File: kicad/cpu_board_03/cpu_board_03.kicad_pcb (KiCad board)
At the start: 4 copper layers, 119.4 x 91.4 mm, 53 parts, among them J1 DIN41612_02x32_AC, J10 PLD_aux, J11 Conn_01x09, J6 Conn_01x02_Socket, J7 Jmp_Irq, J8 Jmp_NMI, J9 Ram1 Enable, SW1 SW_Reset, SW2 SW_PWR, U1 W65C02SxP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

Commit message: routing cpu 3 board
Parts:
- removed J7: Jmp_Irq, Connector_PinHeader_2.54mm:PinHeader_1x02_P2.54mm_Vertical
- removed J8: Jmp_NMI, Connector_PinHeader_2.54mm:PinHeader_1x02_P2.54mm_Vertical
- added C1: 47uF, Capacitor_THT:CP_Radial_D4.0mm_P2.00mm, F.Cu at (122.4, 89.9)
- added R3: 10K, Resistor_SMD:R_0805_2012Metric_Pad1.20x1.40mm_HandSolder, F.Cu at (52.3, 86.4)
- added R5: 10K, Resistor_SMD:R_0805_2012Metric_Pad1.20x1.40mm_HandSolder, F.Cu at (52.3, 88.4)
- C3: footprint Package_SO:SO-20_12.8x7.5mm_P1.27mm -> Capacitor_SMD:C_0805_2012Metric_Pad1.18x1.45mm_HandSolder
- moved SW1 200.6 mm to (26.2, 26.2)
- moved R1 186.5 mm to (33.5, 34.5), turned to -90 degrees
- moved C14 95.8 mm to (87.4, 82.8), turned to -90 degrees
- moved C8 82.0 mm to (71.6, 82.8), turned to -90 degrees
- moved R4 81.0 mm to (41.6, 85.9)
- moved C12 76.0 mm to (129.0, 20.9), turned to -90 degrees
- moved C10 60.4 mm to (-2.56, 74.2)
- moved C3 59.5 mm to (67.1, 79.8), turned to -90 degrees
- moved C7 49.7 mm to (4.06, 84.3)
- moved C11 38.1 mm to (33.9, 90.9)
- moved C4 27.6 mm to (90.9, 17.8), turned to 180 degrees
- moved C6 22.7 mm to (49.3, 17.8), turned to 180 degrees
- moved C5 17.2 mm to (62.5, 17.8), turned to 180 degrees
- moved U9 10.2 mm to (40.6, 63.5)
- moved U10 1.91 mm to (79.4, 86.0)
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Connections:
- J1 pad a10: /AB7 -> VCC
- J1 pad a11: /AB6 -> /AB14
- J1 pad a12: /AB5 -> /AB12
- J1 pad a13: /AB4 -> /AB10
- J1 pad a14: /AB3 -> /AB8
- J1 pad a15: /AB2 -> /AB6
- J1 pad a16: /AB1 -> /AB4
- J1 pad a17: /AB0 -> /AB2
- J1 pad a18: VCC -> /AB0
- J1 pad a2: /AB15 -> /DB6
- J1 pad a21: /~{SYS_CLK} -> unconnected-(J1-Pin_a21-Pada21)
- J1 pad a22: /SYS_CLK -> unconnected-(J1-Pin_a22-Pada22)
- J1 pad a23: /~{IO_SEL} -> /~{IOEN_06}
- J1 pad a24: /~{IOEN_07} -> /~{IOEN_04}
- J1 pad a25: /~{IOEN_06} -> /~{IOEN_02_UART}
- J1 pad a26: /~{IOEN_05} -> /~{IOEN_00_GPIO0}
- J1 pad a27: /~{IOEN_04} -> VCC
- J1 pad a28: /~{IOEN_03} -> unconnected-(J1-Pin_a28-Pada28)
- J1 pad a29: /~{IOEN_02} -> unconnected-(J1-Pin_a29-Pada29)
- J1 pad a3: /AB14 -> /DB4
- J1 pad a30: /~{IOEN_01} -> /~{NMI}
- J1 pad a31: /~{IOEN_00_GPIO0} -> /~{IRQ}
- J1 pad a4: /AB13 -> /DB2
- J1 pad a5: /AB12 -> /DB0
- J1 pad a6: /AB11 -> VCC
- J1 pad a7: /AB10 -> /SYS_CLK
- J1 pad a8: /AB9 -> /~{IO_SEL}
- J1 pad a9: /AB8 -> unconnected-(J1-Pin_a9-Pada9)
- J1 pad c10: unconnected-(J1-Pin_c10-Padc10) -> GND
- J1 pad c11: unconnected-(J1-Pin_c11-Padc11) -> /AB15
- J1 pad c12: unconnected-(J1-Pin_c12-Padc12) -> /AB13
- J1 pad c13: unconnected-(J1-Pin_c13-Padc13) -> /AB11
- J1 pad c14: unconnected-(J1-Pin_c14-Padc14) -> /AB9
- J1 pad c15: unconnected-(J1-Pin_c15-Padc15) -> /AB7
- J1 pad c16: unconnected-(J1-Pin_c16-Padc16) -> /AB5
- J1 pad c17: unconnected-(J1-Pin_c17-Padc17) -> /AB3
- J1 pad c18: GND -> /AB1
- J1 pad c23: unconnected-(J1-Pin_c23-Padc23) -> /~{IOEN_07}
- J1 pad c24: unconnected-(J1-Pin_c24-Padc24) -> /~{IOEN_05}
- J1 pad c25: unconnected-(J1-Pin_c25-Padc25) -> /~{IOEN_03}
- J1 pad c26: unconnected-(J1-Pin_c26-Padc26) -> /~{IOEN_01}
- J1 pad c27: unconnected-(J1-Pin_c27-Padc27) -> GND
- J1 pad c3: /DB6 -> /DB5
- J1 pad c4: /DB5 -> /DB3
- J1 pad c5: /DB4 -> /DB1
- J1 pad c6: /DB3 -> GND
- J1 pad c7: /DB2 -> /~{SYS_CLK}
- J1 pad c8: /DB1 -> /PLD_O7
- J1 pad c9: /DB0 -> /PLD_O0
- U9 pad 7: /CLOCK -> /SYS_CLK
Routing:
- net VCC: track 0.00 -> 268.1 mm
- net /~{IO_SEL}: track 0.00 -> 112.5 mm, vias 0 -> 4
- net /SYS_CLK: track 0.00 -> 100.8 mm, vias 0 -> 4
- net /PLD_O0: track 0.00 -> 77.3 mm
- net /PLD_O7: track 0.00 -> 58.0 mm
- net Net-(U9-~{PB_RST}): track 0.00 -> 52.1 mm
- net /~{SYS_CLK}: track 0.00 -> 51.4 mm
- net /~{RES}: track 0.00 -> 42.3 mm
- net /~{NMI}: track 0.00 -> 34.2 mm
- net /RES: track 0.00 -> 32.7 mm
- net /~{IRQ}: track 0.00 -> 31.8 mm
- net /A6: track 6.13 -> 37.6 mm
- net /A5: track 5.61 -> 35.8 mm
- net /A4: track 5.08 -> 34.3 mm
- net /~{IOEN_00_GPIO0}: track 0.00 -> 22.1 mm
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
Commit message: cleanup and routing
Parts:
- moved C10 64.8 mm to (62.0, 79.8)
- moved U2 8.19 mm to (50.8, 20.3)
- moved C6 8.14 mm to (57.4, 17.3)
- moved U7 7.69 mm to (63.5, 20.3)
- moved C5 7.64 mm to (70.1, 17.3)
- moved U6 4.51 mm to (114.6, 66.2)
- moved U8 4.51 mm to (114.6, 82.4)
- moved H1 4.02 mm to (30.5, 20.3)
- moved H2 1.80 mm to (137.2, 20.3)
- moved C1 1.61 mm to (124.0, 90.4)
- moved SW2 1.61 mm to (226.2, 85.6)
- moved C12 1.61 mm to (130.6, 21.4)
- moved C9 1.61 mm to (221.8, 56.5)
- moved R1 1.61 mm to (35.1, 35.1)
- moved RN1 1.61 mm to (155.8, 47.3)
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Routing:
- net /A12: track 0.00 -> 117.2 mm, vias 0 -> 1
- net /A7: track 6.53 -> 119.9 mm, vias 0 -> 2
- net /A14: track 0.00 -> 102.7 mm, vias 0 -> 2
- net /A13: track 0.00 -> 96.2 mm, vias 0 -> 1
- net /A8: track 6.86 -> 100.5 mm
- net /A11: track 6.55 -> 100.1 mm, vias 0 -> 2
- net /A9: track 6.34 -> 97.3 mm
- net /A10: track 6.02 -> 94.9 mm, vias 0 -> 1
- net /R/~{W}: track 0.00 -> 80.6 mm, vias 0 -> 1
- net /PLD_O0: track 77.3 -> 0.00 mm
- net /A6: track 37.6 -> 114.3 mm, vias 0 -> 2
- net /A5: track 35.8 -> 109.4 mm
- net /A2: track 7.27 -> 76.5 mm
- net /A3: track 6.75 -> 74.8 mm
- net /A4: track 34.3 -> 101.9 mm, vias 0 -> 2
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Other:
- board size 119.4 x 91.4 mm -> 116.8 x 94 mm

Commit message: more routing on cpu board v3
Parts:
- added C13: 100nF, Capacitor_SMD:C_0805_2012Metric_Pad1.18x1.45mm_HandSolder, F.Cu at (118.4, 57.4)
- added C2: 100nF, Capacitor_SMD:C_0805_2012Metric_Pad1.18x1.45mm_HandSolder, F.Cu at (108.2, 17.3)
- moved SW2 187.1 mm to (39.1, 87.9)
- moved D13 176.9 mm to (41.1, 43.2)
- moved R2 176.9 mm to (43.7, 43.2)
- moved C7 116.5 mm to (121.9, 77.7)
- moved C9 101.2 mm to (126.0, 23.9), turned to 0 degrees
- moved J10 98.2 mm to (115.8, 21.8), turned to 90 degrees
- moved J9 92.1 mm to (121.9, 47.2), turned to -90 degrees
- moved D12 41.6 mm to (115.3, 42.2)
- moved RN1 39.4 mm to (129.3, 76.4)
- moved D10 39.2 mm to (117.9, 42.2)
- moved D11 39.2 mm to (120.4, 42.2)
- moved D9 38.3 mm to (122.9, 42.2)
- moved RN3 38.2 mm to (127.0, 41.7), turned to 0 degrees
- moved D1 34.1 mm to (129.0, 73.2), turned to 0 degrees
- moved C12 33.8 mm to (97.0, 16.8)
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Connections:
- RN1 pad 1: Net-(D1-K) -> Net-(D3-K)
- RN1 pad 3: Net-(D3-K) -> Net-(D1-K)
- RN2 pad 2: Net-(D6-K) -> Net-(D8-K)
- RN2 pad 4: Net-(D8-K) -> Net-(D6-K)
- RN3 pad 2: Net-(D11-A) -> Net-(D9-A)
- RN3 pad 3: Net-(D10-A) -> Net-(D11-A)
- RN3 pad 4: Net-(D9-A) -> Net-(D10-A)
- U4 pad 19: /~{CS_RAM0} -> /~{CS_RAM1}
- U4 pad 20: /~{CS_RAM1} -> /~{CS_RAM0}
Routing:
- net GND: track 70.1 -> 685.5 mm, vias 6 -> 18
- net VCC: track 207.4 -> 338.9 mm
- net /PLD_O0: track 0.00 -> 78.8 mm
- net /~{IOEN_00_GPIO0}: track 22.1 -> 98.4 mm, vias 0 -> 6
- net /~{QWE_RAM}: track 0.00 -> 60.8 mm, vias 0 -> 1
- net /A15: track 33.5 -> 92.2 mm, vias 1 -> 2
- net /D0: track 53.2 -> 98.5 mm, vias 0 -> 1
- net /D1: track 53.3 -> 95.6 mm, vias 1 -> 2
- net /D2: track 53.5 -> 92.9 mm, vias 1 -> 2
- net /A14: track 102.7 -> 141.3 mm, vias 2 -> 3
- net /D3: track 62.5 -> 98.7 mm, vias 1 -> 2
- net /CLOCK: track 0.00 -> 36.1 mm, vias 0 -> 1
- net /D4: track 66.5 -> 100.4 mm, vias 1 -> 2
- net /D5: track 71.6 -> 103.1 mm, vias 1 -> 2
- net /D6: track 76.9 -> 105.9 mm, vias 1 -> 2
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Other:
- board size 116.8 x 94 mm -> 104.6 x 92.5 mm

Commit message: more routing
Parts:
- added C15: 100nF, Capacitor_SMD:C_0805_2012Metric_Pad1.18x1.45mm_HandSolder, F.Cu at (52.8, 79.8)
- added U12: 74LS138, Package_SO:SO-16_3.9x9.9mm_P1.27mm, F.Cu at (51.0, 87.0)
- moved R5 16.0 mm to (46.5, 74.7), turned to 0 degrees
- moved R1 15.9 mm to (41.9, 41.7), turned to 180 degrees
- moved R2 15.0 mm to (39.9, 57.7)
- moved D13 14.5 mm to (42.4, 57.7)
- moved R3 12.0 mm to (46.5, 77.5), turned to 0 degrees
- moved C9 10.2 mm to (115.8, 23.9), turned to 90 degrees
- moved SW1 5.15 mm to (43.4, 46.0), turned to -90 degrees
- moved J9 5.06 mm to (116.8, 47.2), turned to 90 degrees
- moved C11 3.01 mm to (40.6, 75.7), turned to 180 degrees
- moved J10 2.26 mm to (115.8, 19.6)
- moved C10 1.08 mm to (62.7, 80.0)
- moved U5 1.05 mm to (61.2, 87.0)
- moved SW2 1.02 mm to (38.1, 87.9), turned to -90 degrees
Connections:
- J1 pad a19: unconnected-(J1-Pin_a19-Pada19) -> VCC
- J1 pad a21: unconnected-(J1-Pin_a21-Pada21) -> /~{IOEN_06}
- J1 pad a22: unconnected-(J1-Pin_a22-Pada22) -> /~{IOEN_04}
- J1 pad a23: /~{IOEN_06} -> /~{IOEN_02_UART}
- J1 pad a24: /~{IOEN_04} -> /~{IOEN_00_GPIO0}
- J1 pad a25: /~{IOEN_02_UART} -> /~{IOEN_14}
- J1 pad a26: /~{IOEN_00_GPIO0} -> /~{IOEN_12}
- J1 pad a27: VCC -> /~{IOEN_10}
- J1 pad a28: unconnected-(J1-Pin_a28-Pada28) -> /~{IOEN_08}
- J1 pad a29: unconnected-(J1-Pin_a29-Pada29) -> VCC
- J1 pad a30: /~{NMI} -> /~{IRQ}
- J1 pad a31: /~{IRQ} -> /~{RES}
- J1 pad c19: unconnected-(J1-Pin_c19-Padc19) -> GND
- J1 pad c21: unconnected-(J1-Pin_c21-Padc21) -> /~{IOEN_07}
- J1 pad c22: unconnected-(J1-Pin_c22-Padc22) -> /~{IOEN_05}
- J1 pad c23: /~{IOEN_07} -> /~{IOEN_03}
- J1 pad c24: /~{IOEN_05} -> /~{IOEN_01}
- J1 pad c25: /~{IOEN_03} -> /~{IOEN_15}
- J1 pad c26: /~{IOEN_01} -> /~{IOEN_13}
- J1 pad c27: GND -> /~{IOEN_11}
- J1 pad c28: unconnected-(J1-Pin_c28-Padc28) -> /~{IOEN_09}
- J1 pad c29: unconnected-(J1-Pin_c29-Padc29) -> GND
- J1 pad c30: /RES -> /~{NMI}
- J1 pad c31: /~{RES} -> /RES
- J1 pad c8: /PLD_O7 -> /~{IO_RD_DIR}
- J10 pad 1: /PLD_I1 -> GND
- J10 pad 2: /PLD_O0 -> /PLD_I1
- J10 pad 3: /PLD_O7 -> VCC
- J9 pad 1: VCC -> GND
- J9 pad 3: GND -> VCC
- U10 pad 1: GND -> VCC
- U11 pad 1: GND -> VCC
- U4 pad 16: /PLD_O7 -> /~{IO_RD_DIR}
- U8 pad 1: unconnected-(U8-A->B-Pad1) -> /~{IO_RD_DIR}
- U8 pad 19: unconnected-(U8-CE-Pad19) -> GND
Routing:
- net VCC: track 338.9 -> 598.9 mm, vias 0 -> 2
- net /~{IO_RD_DIR}: track 0.00 -> 62.7 mm, vias 0 -> 2
- net /PLD_O7: track 58.0 -> 0.00 mm
- net /~{RES}: track 8.08 -> 53.8 mm
- net /RES: track 0.00 -> 31.4 mm
- net /PLD_I1: track 0.00 -> 26.2 mm
- net Net-(U9-~{PB_RST}): track 0.00 -> 23.9 mm
- net /~{IOEN_08}: track 0.00 -> 21.4 mm
- net /~{IOEN_10}: track 0.00 -> 18.6 mm
- net /~{IOEN_12}: track 0.00 -> 16.7 mm
- net /~{IOEN_15}: track 0.00 -> 15.6 mm, vias 0 -> 2
- net /~{IO_SEL}: track 113.9 -> 129.0 mm, vias 4 -> 5
- net /~{IOEN_09}: track 0.00 -> 14.4 mm
- net /A6: track 114.3 -> 127.9 mm, vias 2 -> 3
- net /~{QWE_RAM}: track 60.8 -> 74.3 mm
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
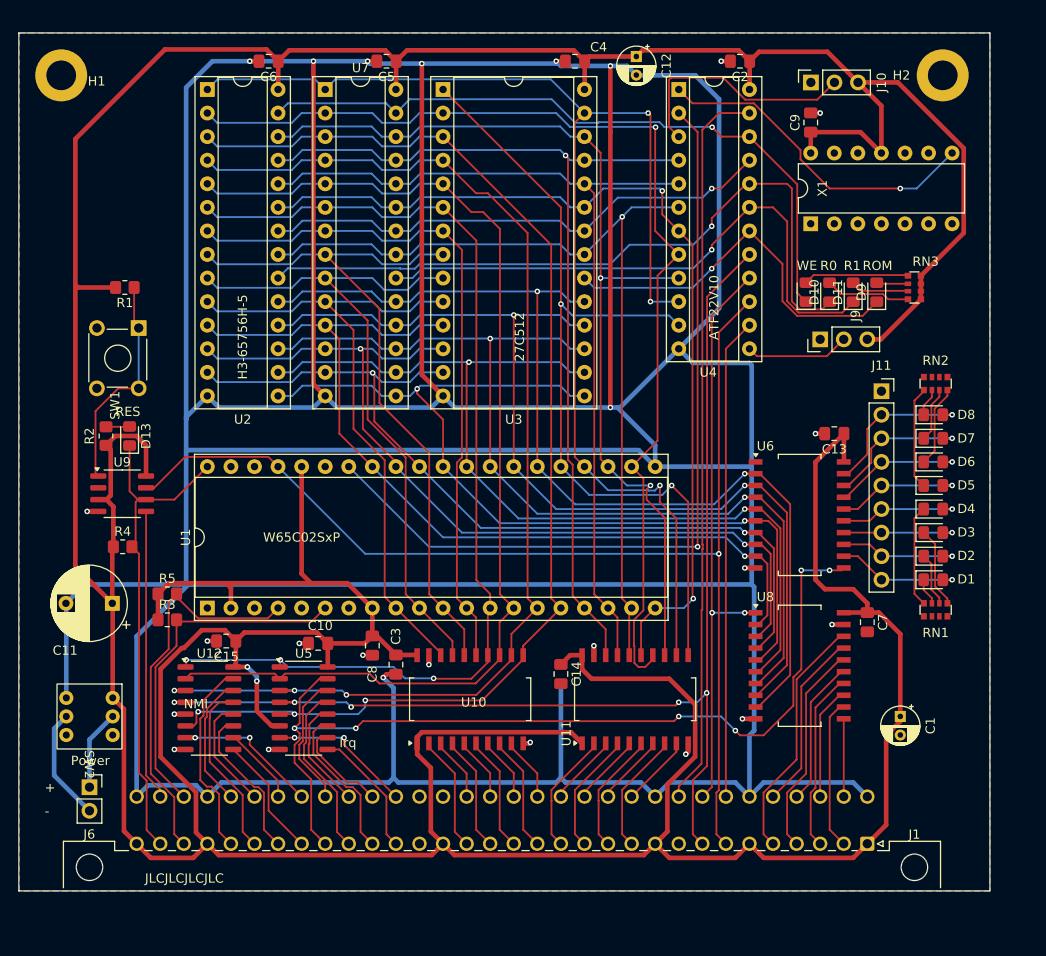
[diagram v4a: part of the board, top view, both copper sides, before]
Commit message: shrink board
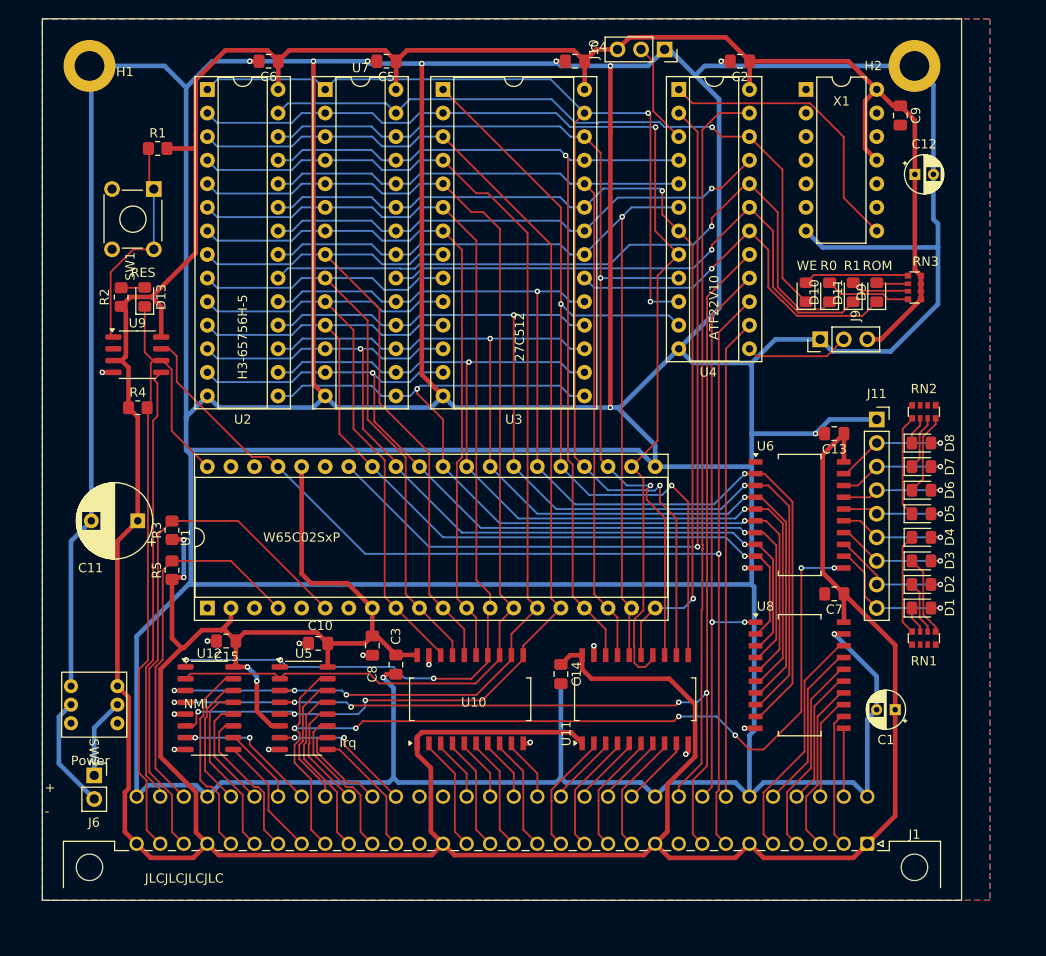
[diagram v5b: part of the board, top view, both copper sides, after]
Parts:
- moved C12 32.6 mm to (127.0, 29.5), turned to 0 degrees
- moved J10 16.2 mm to (100.1, 16.0), turned to -90 degrees
- moved R1 15.4 mm to (45.5, 26.7), turned to 0 degrees
- moved D13 15.1 mm to (44.1, 42.7)
- moved R2 15.1 mm to (41.5, 42.7)
- moved R4 15.1 mm to (43.3, 54.6)
- moved SW1 15.1 mm to (45.0, 31.0)
- moved U9 15.1 mm to (43.3, 48.9)
- moved X1 14.5 mm to (115.3, 20.3), turned to 0 degrees
- moved C9 9.68 mm to (125.5, 23.1), turned to -90 degrees
- moved R3 9.67 mm to (47.0, 67.8), turned to 90 degrees
- moved C11 9.30 mm to (43.3, 66.8)
- moved C7 4.68 mm to (118.4, 74.7), turned to 180 degrees
- moved D5 3.30 mm to (127.8, 66.0)
- moved RN1 3.30 mm to (128.0, 79.4)
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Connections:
- J1 pad a30: /~{IRQ} -> /~{NMI}
- J1 pad c30: /~{NMI} -> /~{IRQ}
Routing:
- net GND: track 676.0 -> 854.2 mm, vias 25 -> 24
- net VCC: track 598.9 -> 548.0 mm, vias 2 -> 4
- net /~{RES}: track 53.8 -> 74.4 mm
- net /~{NMI}: track 37.9 -> 57.7 mm
- net /RES: track 31.4 -> 47.3 mm
- net /PLD_I1: track 26.2 -> 11.1 mm
- net /CLOCK: track 36.1 -> 31.5 mm, vias 1 -> 0
- net /GPIO00_O7: track 16.9 -> 12.8 mm
- net /GPIO00_O6: track 15.7 -> 12.3 mm
- net /SYS_CLK: track 127.8 -> 131.2 mm
- net /GPIO00_O5: track 14.3 -> 11.7 mm
- net /~{CS_RAM0}: track 76.9 -> 74.5 mm
- net /~{IOEN_00_GPIO0}: track 97.6 -> 99.9 mm
- net /GPIO00_O4: track 13.8 -> 11.6 mm
- net /D6: track 105.9 -> 107.9 mm
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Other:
- board size 104.6 x 92.5 mm -> 99.1 x 95 mm

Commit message: DRCs pass...
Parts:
- moved U12 14.5 mm to (65.4, 88.4), turned to 90 degrees
- moved C10 13.9 mm to (49.0, 82.3), turned to 90 degrees
- moved C15 8.52 mm to (61.0, 82.3), turned to 90 degrees
- moved U5 7.83 mm to (53.5, 88.4), turned to 90 degrees
- moved C3 1.61 mm to (67.6, 79.0), turned to 180 degrees
- moved C8 1.44 mm to (70.1, 81.3), turned to 180 degrees
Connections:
- J1 pad a21: /~{IOEN_06} -> /~{IOEN_14}
- J1 pad a22: /~{IOEN_04} -> /~{IOEN_12}
- J1 pad a23: /~{IOEN_02_UART} -> /~{IOEN_10}
- J1 pad a24: /~{IOEN_00_GPIO0} -> /~{IOEN_08}
- J1 pad a25: /~{IOEN_14} -> /~{IOEN_06}
- J1 pad a26: /~{IOEN_12} -> /~{IOEN_04}
- J1 pad a27: /~{IOEN_10} -> /~{IOEN_02_UART}
- J1 pad a28: /~{IOEN_08} -> /~{IOEN_00_GPIO0}
- J1 pad c21: /~{IOEN_07} -> /~{IOEN_15}
- J1 pad c22: /~{IOEN_05} -> /~{IOEN_13}
- J1 pad c23: /~{IOEN_03} -> /~{IOEN_11}
- J1 pad c24: /~{IOEN_01} -> /~{IOEN_09}
- J1 pad c25: /~{IOEN_15} -> /~{IOEN_07}
- J1 pad c26: /~{IOEN_13} -> /~{IOEN_05}
- J1 pad c27: /~{IOEN_11} -> /~{IOEN_03}
- J1 pad c28: /~{IOEN_09} -> /~{IOEN_01}
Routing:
- net GND: track 854.2 -> 882.0 mm, vias 24 -> 23
- net /~{IOEN_00_GPIO0}: track 99.9 -> 123.7 mm, vias 6 -> 1
- net /~{IOEN_15}: track 15.6 -> 7.24 mm
- net VCC: track 548.0 -> 555.4 mm
- net /~{IOEN_07}: track 15.6 -> 8.42 mm
- net /~{IO_SEL}: track 129.0 -> 124.2 mm
- net /~{IOEN_08}: track 21.4 -> 16.7 mm
- net /A7: track 132.6 -> 128.3 mm
- net /~{IOEN_14}: track 13.2 -> 16.6 mm
- net /A4: track 114.0 -> 117.4 mm
- net /~{IOEN_09}: track 14.4 -> 11.2 mm
- net /~{IOEN_06}: track 14.0 -> 17.1 mm
- net /~{IOEN_01}: track 14.4 -> 11.5 mm
- net /~{IOEN_13}: track 8.45 -> 11.2 mm
- net /A5: track 119.0 -> 121.5 mm, vias 0 -> 3
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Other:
- board size 99.1 x 95 mm -> 99.1 x 94.2 mm
- board text removed: "Irq"
- board text removed: "NMI"

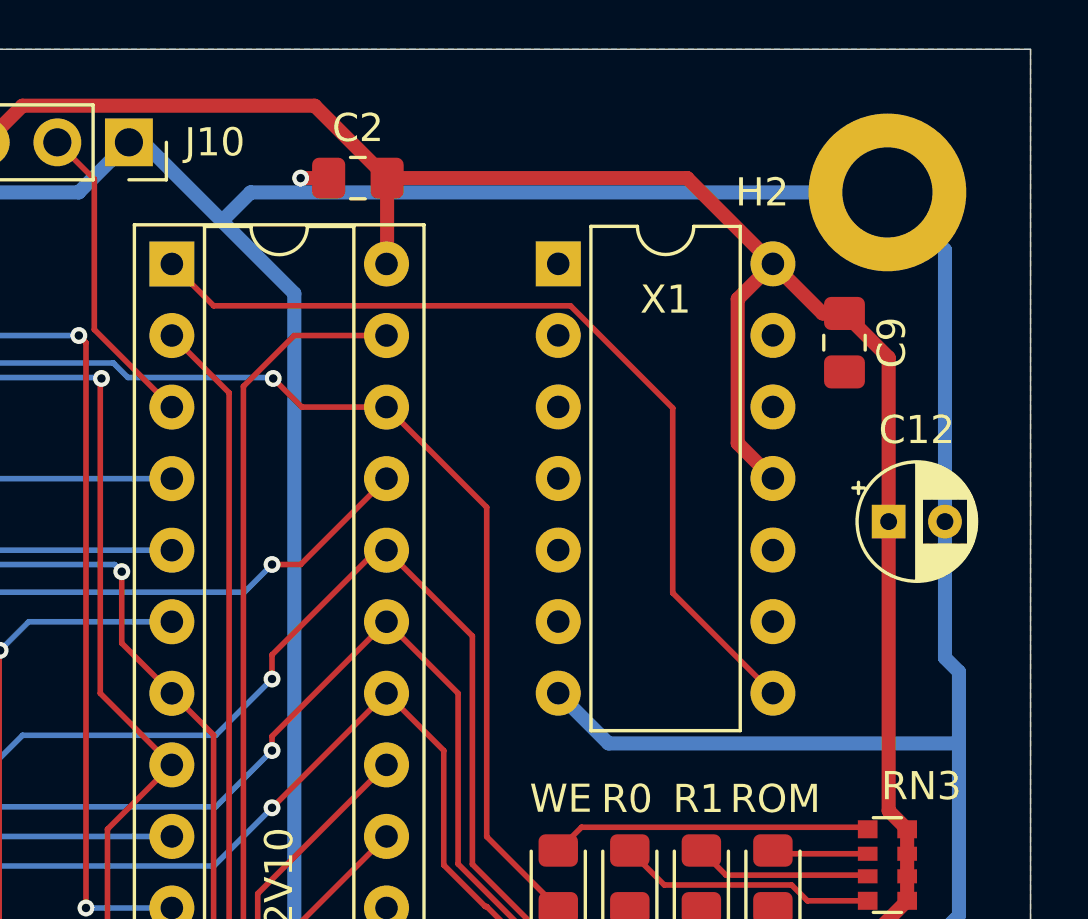
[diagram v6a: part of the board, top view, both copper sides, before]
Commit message: use socket footprint for xtal
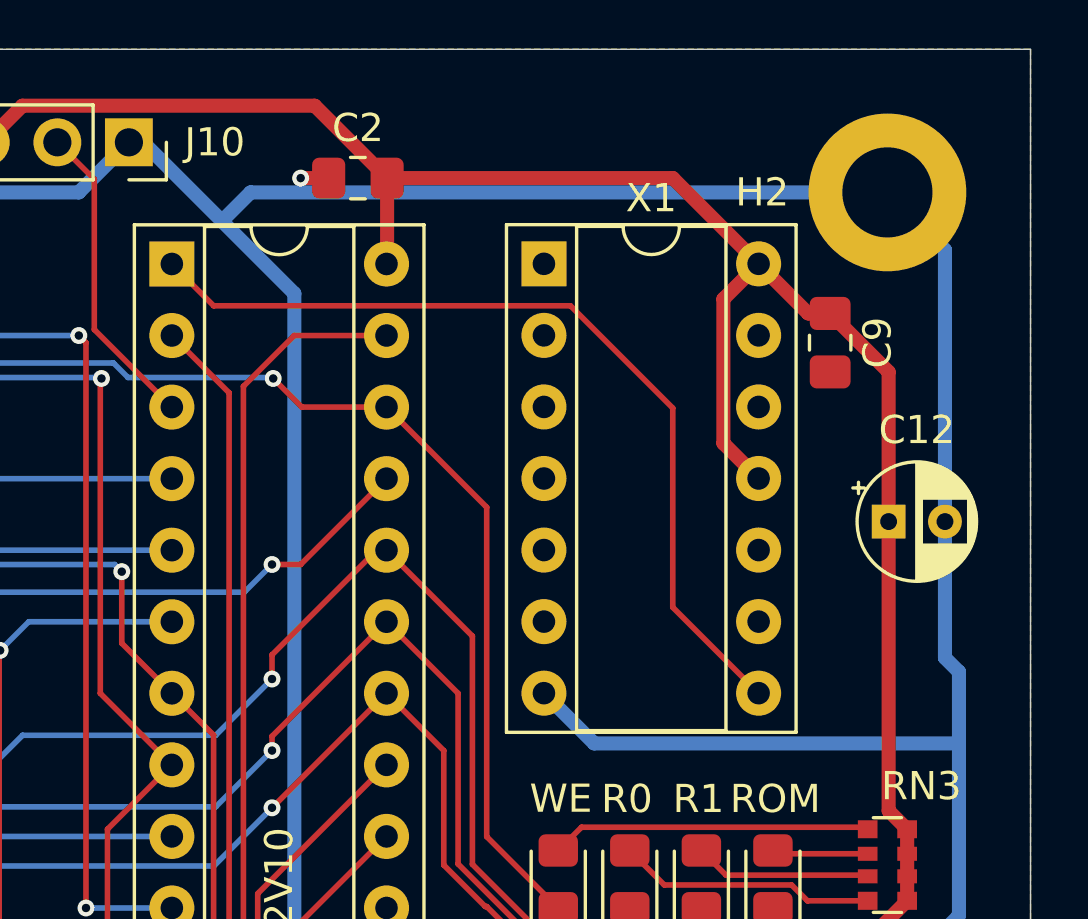
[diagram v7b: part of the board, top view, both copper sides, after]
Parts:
- X1: footprint Package_DIP:DIP-14_W7.62mm -> Package_DIP:DIP-14_W7.62mm_Socket
- moved C9 0.51 mm to (125.0, 23.1)
- moved X1 0.51 mm to (114.8, 20.3)
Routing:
- net GND: track 882.0 -> 882.6 mm
